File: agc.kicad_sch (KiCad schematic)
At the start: 35 parts, among them U1101 DG449DS-T1-E3, U1102 LMC6482, U1103 LMC6482

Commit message: Update pcb database to version 6
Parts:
- C1101, C1105, C1106, C1107, C1108: symbol Custom:C_US_0805_0.1UF_X7R_10%_50V_HS -> custom:C_US_0805_0.1UF_X7R_10%_50V_HS
- C1102, C1103, C1109: symbol Custom:CP_US -> custom:CP_US; PartNumber 800267-226 -> 80000X-XXX
- C1104: symbol Custom:CP_US -> custom:CP_US; PartNumber 800268-107 -> 80000X-XXX
- C1110: symbol Custom:C_US_0805_0.1UF_X7R_10%_50V_HS -> custom:C_US_0805_0.1UF_X7R_10%_50V_HS; PartNumber 800238-105 -> 800238-104
- C1111, C1112: symbol Custom:C_US -> custom:C_US; PartNumber 800003-475 -> 800063-XXX
- CR1101, CR1102, CR1103, CR1104: symbol Custom:BAT54 -> custom:BAT54
- R1101, R1102, R1106, R1107, R1110, R1111, R1113, R1114: symbol Custom:R_US_0805_1%_HS -> custom:R_US_0805_1%_HS; PartNumber 800235-103 -> 800235-XXX
- R1103: symbol Custom:R_US_0805_1%_HS -> custom:R_US_0805_1%_HS; PartNumber 800235-101 -> 800235-XXX
- R1104, R1108: symbol Custom:R_US_0805_1%_HS -> custom:R_US_0805_1%_HS; PartNumber 800235-104 -> 800235-XXX
- R1105: symbol Custom:R_US_0805_1%_HS -> custom:R_US_0805_1%_HS; PartNumber 800235-225 -> 800235-XXX
- R1109: symbol Custom:R_US_0805_1%_HS -> custom:R_US_0805_1%_HS; PartNumber 800235-102 -> 800235-XXX
- R1112: symbol Custom:R_US_0805_1%_HS -> custom:R_US_0805_1%_HS; PartNumber 800235-471 -> 800235-XXX
- TP1101, TP1102: symbol Custom:TESTPINTPSQ025 -> custom:TESTPINTPSQ025
- U1101: symbol Custom:DG449DS-T1-E3 -> custom:DG449DS-T1-E3
- U1102, U1103: symbol Custom:LMC6482 -> custom:LMC6482

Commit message: Fix BOM part number errors and out of sync footprints which happened during conversion from Kicad 5 to 6
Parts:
- C1102, C1103, C1109: PartNumber 80000X-XXX -> 800267-226
- C1104: PartNumber 80000X-XXX -> 800268-107
- C1110: PartNumber 800238-104 -> 800238-105
- C1111, C1112: PartNumber 800063-XXX -> 800003-475
- R1101, R1102, R1106, R1107, R1110, R1111, R1113, R1114: PartNumber 800235-XXX -> 800235-103
- R1103: PartNumber 800235-XXX -> 800235-101
- R1104, R1108: PartNumber 800235-XXX -> 800235-104
- R1105: PartNumber 800235-XXX -> 800235-225
- R1109: PartNumber 800235-XXX -> 800235-102
- R1112: PartNumber 800235-XXX -> 800235-471
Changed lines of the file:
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@@
       (effects (font (size 1.524 1.524)))
     )
-    (property "PartNumber" "80000X-XXX" (id 4) (at 92.71 40.64 0)
+    (property "PartNumber" "800267-226" (id 4) (at 92.71 40.64 0)
       (effects (font (size 1.524 1.524)) hide)
     )
@@
       (effects (font (size 1.524 1.524)))
     )
-    (property "PartNumber" "800235-XXX" (id 4) (at 84.582 73.66 90)
+    (property "PartNumber" "800235-104" (id 4) (at 84.582 73.66 90)
       (effects (font (size 1.524 1.524)) hide)
     )
@@
       (effects (font (size 1.524 1.524)))
     )
-    (property "PartNumber" "800235-XXX" (id 4) (at 38.608 53.34 90)
+    (property "PartNumber" "800235-101" (id 4) (at 38.608 53.34 90)
       (effects (font (size 1.524 1.524)) hide)
     )
@@
       (effects (font (size 1.524 1.524)))
     )
-    (property "PartNumber" "80000X-XXX" (id 4) (at 46.99 62.23 0)
+    (property "PartNumber" "800268-107" (id 4) (at 46.99 62.23 0)
       (effects (font (size 1.524 1.524)) hide)
     )
@@
       (effects (font (size 1.524 1.524)))
     )
-    (property "PartNumber" "800235-XXX" (id 4) (at 96.52 117.602 90)
+    (property "PartNumber" "800235-104" (id 4) (at 96.52 117.602 90)
       (effects (font (size 1.524 1.524)) hide)
     )
@@
       (effects (font (size 1.524 1.524)))
     )
-    (property "PartNumber" "800235-XXX" (id 4) (at 69.85 117.602 90)
+    (property "PartNumber" "800235-103" (id 4) (at 69.85 117.602 90)
       (effects (font (size 1.524 1.524)) hide)
     )
@@
       (effects (font (size 1.524 1.524)))
     )
-    (property "PartNumber" "80000X-XXX" (id 4) (at 57.15 116.84 0)
+    (property "PartNumber" "800267-226" (id 4) (at 57.15 116.84 0)
       (effects (font (size 1.524 1.524)) hide)
     )
@@
       (effects (font (size 1.524 1.524)))
     )
-    (property "PartNumber" "800235-XXX" (id 4) (at 140.97 129.032 90)
+    (property "PartNumber" "800235-103" (id 4) (at 140.97 129.032 90)
       (effects (font (size 1.524 1.524)) hide)
     )
@@
       (effects (font (size 1.524 1.524)))
     )
-    (property "PartNumber" "800235-XXX" (id 4) (at 120.65 112.522 90)
+    (property "PartNumber" "800235-103" (id 4) (at 120.65 112.522 90)
       (effects (font (size 1.524 1.524)) hide)
     )
@@
       (effects (font (size 1.524 1.524)))
     )
-    (property "PartNumber" "800235-XXX" (id 4) (at 173.228 83.82 90)
+    (property "PartNumber" "800235-225" (id 4) (at 173.228 83.82 90)
       (effects (font (size 1.524 1.524)) hide)
     )
@@
       (effects (font (size 1.524 1.524)))
     )
-    (property "PartNumber" "800235-XXX" (id 4) (at 182.372 115.57 90)
+    (property "PartNumber" "800235-102" (id 4) (at 182.372 115.57 90)
       (effects (font (size 1.524 1.524)) hide)
     )
@@
       (effects (font (size 1.524 1.524)))
     )
-    (property "PartNumber" "800238-104" (id 4) (at 177.8 120.65 0)
+    (property "PartNumber" "800238-105" (id 4) (at 177.8 120.65 0)
       (effects (font (size 1.524 1.524)) hide)
     )
@@
       (effects (font (size 1.524 1.524)))
     )
-    (property "PartNumber" "800235-XXX" (id 4) (at 211.328 151.13 90)
+    (property "PartNumber" "800235-103" (id 4) (at 211.328 151.13 90)
       (effects (font (size 1.524 1.524)) hide)
     )
@@
       (effects (font (size 1.524 1.524)))
     )
-    (property "PartNumber" "800063-XXX" (id 4) (at 69.85 167.64 0)
+    (property "PartNumber" "800003-475" (id 4) (at 69.85 167.64 0)
       (effects (font (size 1.524 1.524)) hide)
     )
@@
       (effects (font (size 1.524 1.524)))
     )
-    (property "PartNumber" "800235-XXX" (id 4) (at 80.01 172.212 90)
+    (property "PartNumber" "800235-103" (id 4) (at 80.01 172.212 90)
       (effects (font (size 1.524 1.524)) hide)
     )
@@
       (effects (font (size 1.524 1.524)))
     )
-    (property "PartNumber" "800235-XXX" (id 4) (at 120.65 191.262 90)
+    (property "PartNumber" "800235-103" (id 4) (at 120.65 191.262 90)
       (effects (font (size 1.524 1.524)) hide)
     )
@@
       (effects (font (size 1.524 1.524)))
     )
-    (property "PartNumber" "800063-XXX" (id 4) (at 166.37 165.1 0)
+    (property "PartNumber" "800003-475" (id 4) (at 166.37 165.1 0)
       (effects (font (size 1.524 1.524)) hide)
     )
@@
       (effects (font (size 1.524 1.524)))
     )
-    (property "PartNumber" "800235-XXX" (id 4) (at 196.85 37.592 90)
+    (property "PartNumber" "800235-103" (id 4) (at 196.85 37.592 90)
       (effects (font (size 1.524 1.524)) hide)
     )
@@
       (effects (font (size 1.524 1.524)))
     )
-    (property "PartNumber" "800235-XXX" (id 4) (at 227.33 37.592 90)
+    (property "PartNumber" "800235-103" (id 4) (at 227.33 37.592 90)
       (effects (font (size 1.524 1.524)) hide)
     )
@@
       (effects (font (size 1.524 1.524)))
     )
-    (property "PartNumber" "80000X-XXX" (id 4) (at 213.36 36.83 0)
+    (property "PartNumber" "800267-226" (id 4) (at 213.36 36.83 0)
       (effects (font (size 1.524 1.524)) hide)
     )
@@
       (effects (font (size 1.524 1.524)))
     )
-    (property "PartNumber" "800235-XXX" (id 4) (at 179.07 164.592 90)
-      (effects (font (size 1.524 1.524)) hide)
-    )
+    (property "PartNumber" "800235-471" (id 4) (at 179.07 164.592 90)
+      (effects (font (size 1.524 1.524)) hide)
+    )

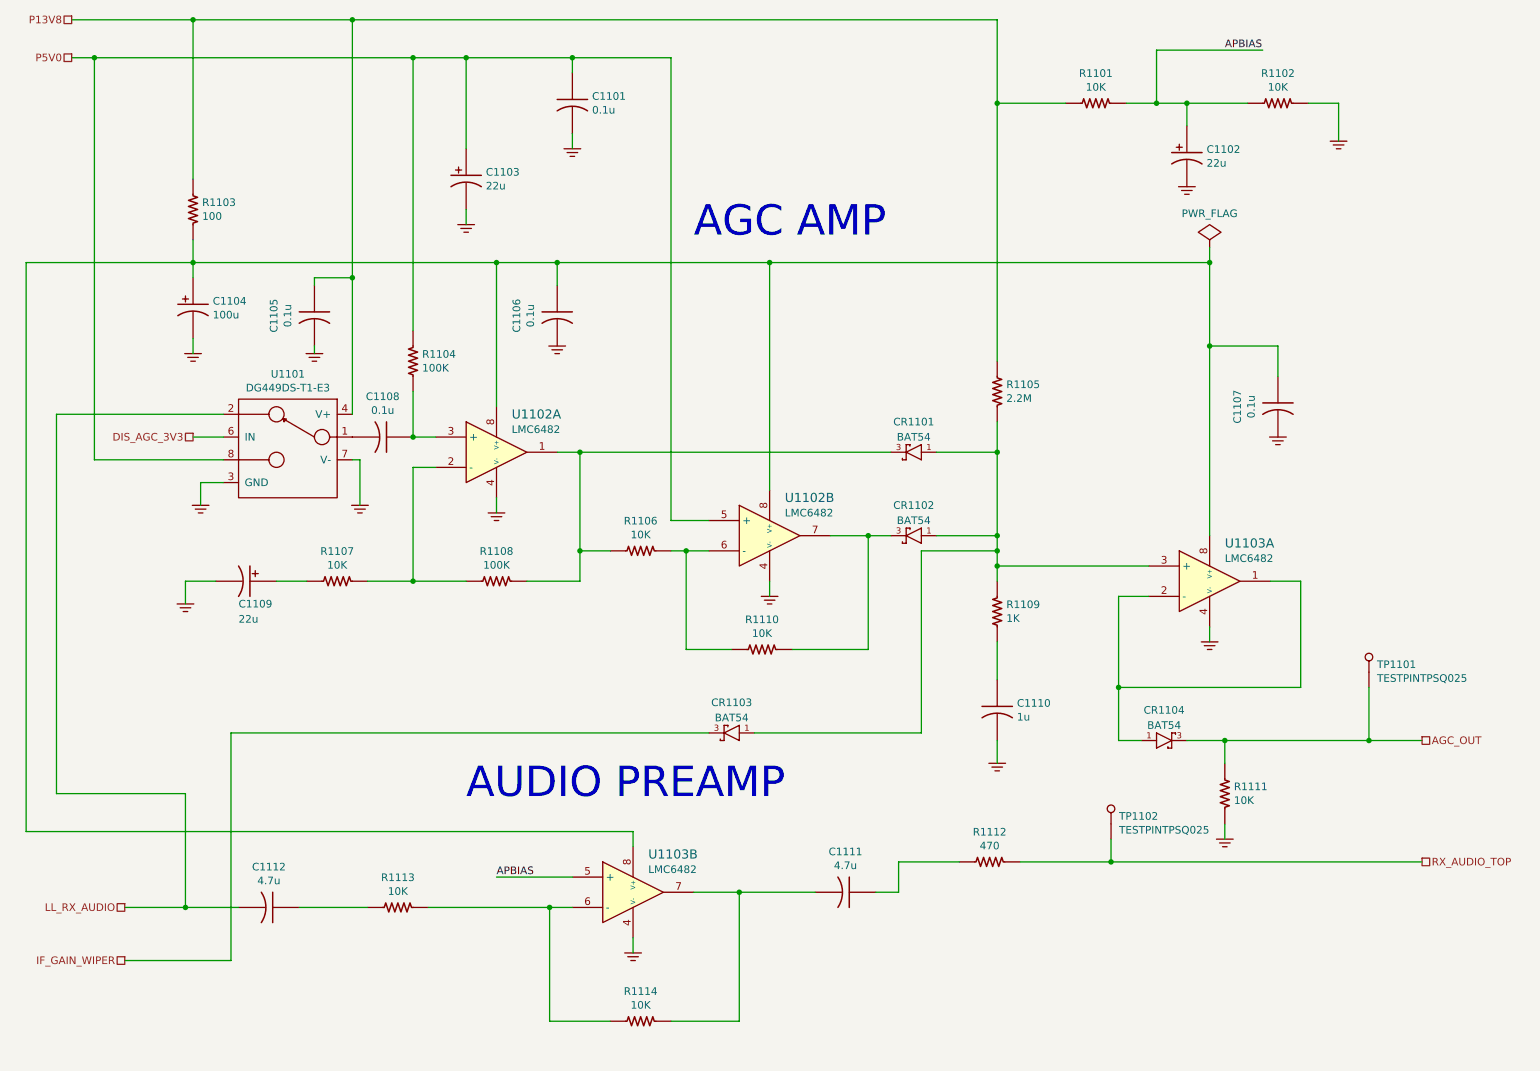
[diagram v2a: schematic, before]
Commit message: trx_mobo_concept_2_B. Change design to use a dedicated 8V supply for the 2SC3357 parts. Add S-Meter connector. Change mic connector to 3 pins and add 8V sopower supply to pin 3.
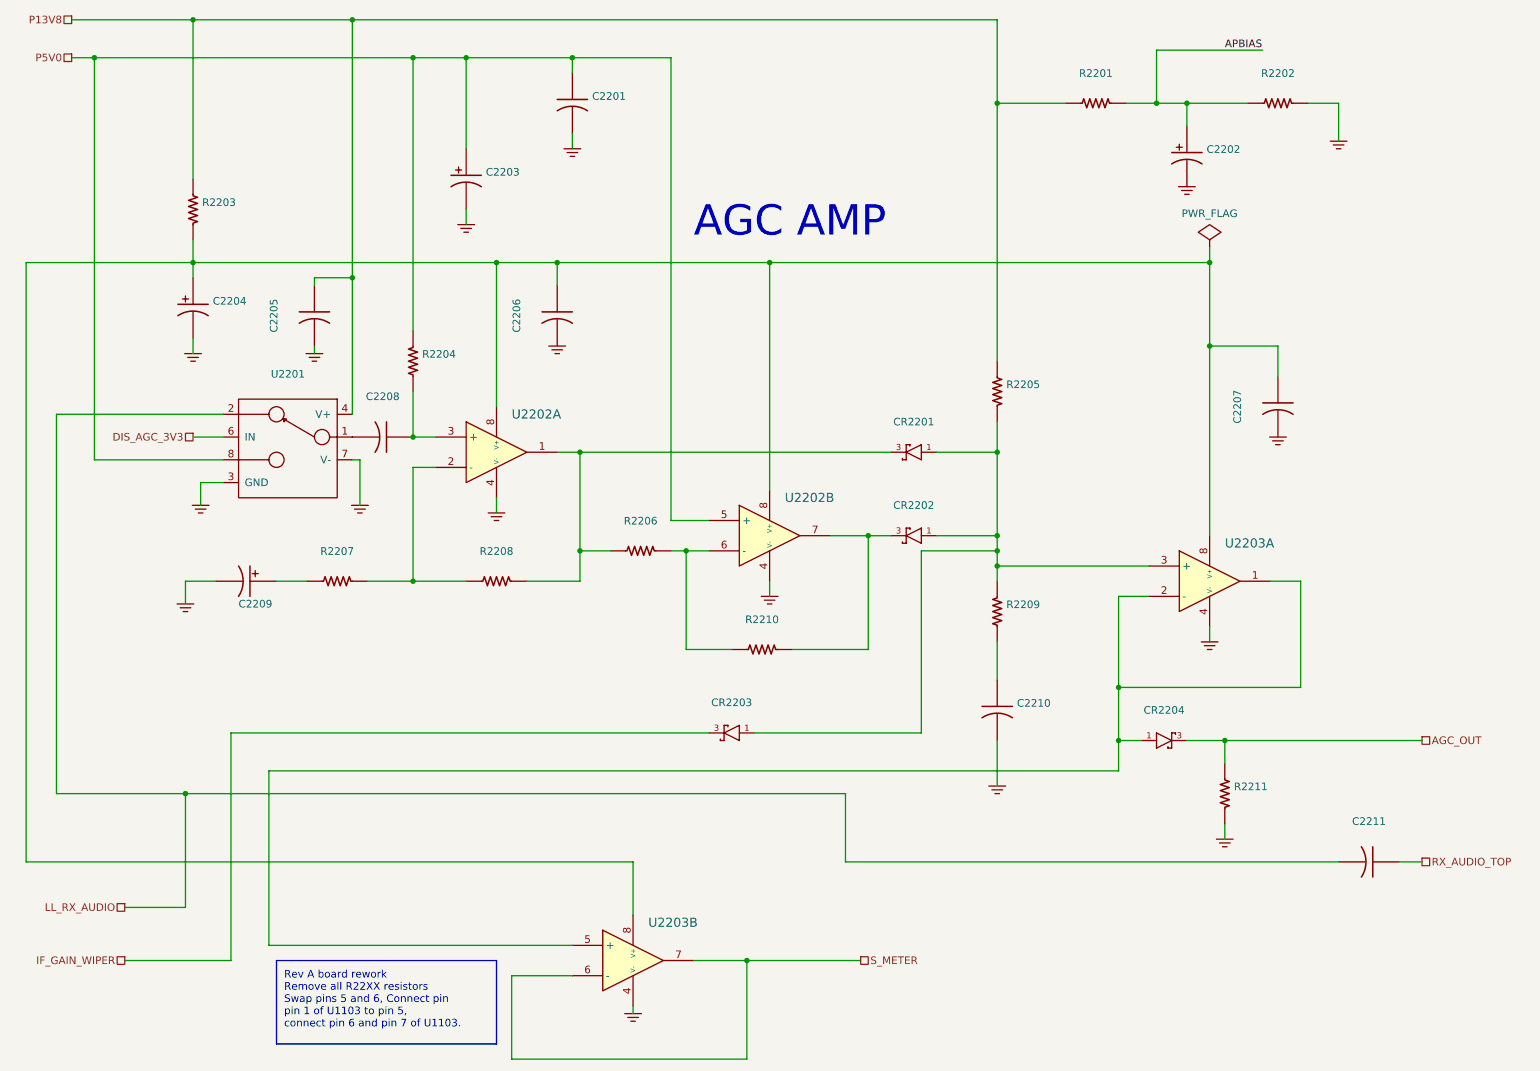
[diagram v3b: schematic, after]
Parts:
- removed C1111: 4.7u, Capacitor_SMD:C_0805_2012Metric_Pad1.15x1.40mm_HandSolder, symbol custom:C_US
- removed R1112: 470, Resistor_SMD:R_0805_2012Metric_Pad1.15x1.40mm_HandSolder, symbol custom:R_US_0805_1%_HS
- removed R1113, R1114: 10K, Resistor_SMD:R_0805_2012Metric_Pad1.15x1.40mm_HandSolder, symbol custom:R_US_0805_1%_HS
- removed TP1101, TP1102: TESTPINTPSQ025, mods:TESTPIN, symbol custom:TESTPINTPSQ025
- C2201: renamed from C1101; value 0.1u -> (none); footprint Capacitor_SMD:C_0805_2012Metric_Pad1.15x1.40mm_HandSolder -> (none)
- C2202: renamed from C1102; value 22u -> (none); footprint Capacitor_SMD:CP_Elec_6.3x5.7 -> (none)
- C2203: renamed from C1103; value 22u -> (none); footprint Capacitor_SMD:CP_Elec_6.3x5.7 -> (none)
- C2204: renamed from C1104; value 100u -> (none); footprint Capacitor_SMD:CP_Elec_8x10 -> (none)
- C2205: renamed from C1105; value 0.1u -> (none); footprint Capacitor_SMD:C_0805_2012Metric_Pad1.15x1.40mm_HandSolder -> (none)
- C2206: renamed from C1106; value 0.1u -> (none); footprint Capacitor_SMD:C_0805_2012Metric_Pad1.15x1.40mm_HandSolder -> (none)
- C2207: renamed from C1107; value 0.1u -> (none); footprint Capacitor_SMD:C_0805_2012Metric_Pad1.15x1.40mm_HandSolder -> (none)
- C2208: renamed from C1108; value 0.1u -> (none); footprint Capacitor_SMD:C_0805_2012Metric_Pad1.15x1.40mm_HandSolder -> (none)
- C2209: renamed from C1109; value 22u -> (none); footprint Capacitor_SMD:CP_Elec_6.3x5.7 -> (none)
- C2210: renamed from C1110; value 1u -> (none); footprint Capacitor_SMD:C_0805_2012Metric_Pad1.15x1.40mm_HandSolder -> (none)
- C2211: renamed from C1112; value 4.7u -> (none); footprint Capacitor_SMD:C_0805_2012Metric_Pad1.15x1.40mm_HandSolder -> (none)
- CR2201: renamed from CR1101; value BAT54 -> (none); footprint mods:SOT23-3-SAR -> (none)
- CR2202: renamed from CR1102; value BAT54 -> (none); footprint mods:SOT23-3-SAR -> (none)
- CR2203: renamed from CR1103; value BAT54 -> (none); footprint mods:SOT23-3-SAR -> (none)
- CR2204: renamed from CR1104; value BAT54 -> (none); footprint mods:SOT23-3-SAR -> (none)
- R2201: renamed from R1101; value 10K -> (none); footprint Resistor_SMD:R_0805_2012Metric_Pad1.15x1.40mm_HandSolder -> (none)
- R2202: renamed from R1102; value 10K -> (none); footprint Resistor_SMD:R_0805_2012Metric_Pad1.15x1.40mm_HandSolder -> (none)
- R2203: renamed from R1103; value 100 -> (none); footprint Resistor_SMD:R_0805_2012Metric_Pad1.15x1.40mm_HandSolder -> (none)
- R2204: renamed from R1104; value 100K -> (none); footprint Resistor_SMD:R_0805_2012Metric_Pad1.15x1.40mm_HandSolder -> (none)
- R2205: renamed from R1105; value 2.2M -> (none); footprint Resistor_SMD:R_0805_2012Metric_Pad1.15x1.40mm_HandSolder -> (none)
- R2206: renamed from R1106; value 10K -> (none); footprint Resistor_SMD:R_0805_2012Metric_Pad1.15x1.40mm_HandSolder -> (none)
- R2207: renamed from R1107; value 10K -> (none); footprint Resistor_SMD:R_0805_2012Metric_Pad1.15x1.40mm_HandSolder -> (none)
- R2208: renamed from R1108; value 100K -> (none); footprint Resistor_SMD:R_0805_2012Metric_Pad1.15x1.40mm_HandSolder -> (none)
- R2209: renamed from R1109; value 1K -> (none); footprint Resistor_SMD:R_0805_2012Metric_Pad1.15x1.40mm_HandSolder -> (none)
- R2210: renamed from R1110; value 10K -> (none); footprint Resistor_SMD:R_0805_2012Metric_Pad1.15x1.40mm_HandSolder -> (none)
- R2211: renamed from R1111; value 10K -> (none); footprint Resistor_SMD:R_0805_2012Metric_Pad1.15x1.40mm_HandSolder -> (none)
- U2201: renamed from U1101; value DG449DS-T1-E3 -> (none); footprint Package_TO_SOT_SMD:SOT-23-8_Handsoldering -> (none)
- U2202: renamed from U1102; value LMC6482 -> (none); footprint mods:SOIC8N-SAR -> (none)
- U2203: renamed from U1103; value LMC6482 -> (none); footprint mods:SOIC8N-SAR -> (none)
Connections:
- net APBIAS: no longer U2203.5 (+)
- net RX_AUDIO_TOP: now also C2211.1
- net at CR2204.1 (A), U2203.1, U2203.2 (-): now also U2203.5 (+)
- net S_METER: now reaches U2203.6 (-)
- net S_METER: now also U2203.7
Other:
- note added: "Rev A board rework Remove all R22XX resistors Swap pins 5 and 6, Connect pin pin 1 of U1103 to pin 5, connect pin 6 and pin 7 of U1103."
- note removed: "AUDIO PREAMP"
- moved on the sheet: C2211, U2203B
